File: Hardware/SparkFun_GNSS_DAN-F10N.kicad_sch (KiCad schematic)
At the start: 52 parts, among them J1 USB_C_Receptacle, J2 Conn_01x06, J4 U.FL, J5 Conn_01x08, U1 DT1042-04SO, U3 RT9080-3.3, U4 CH340C, U5 DAN-F10N

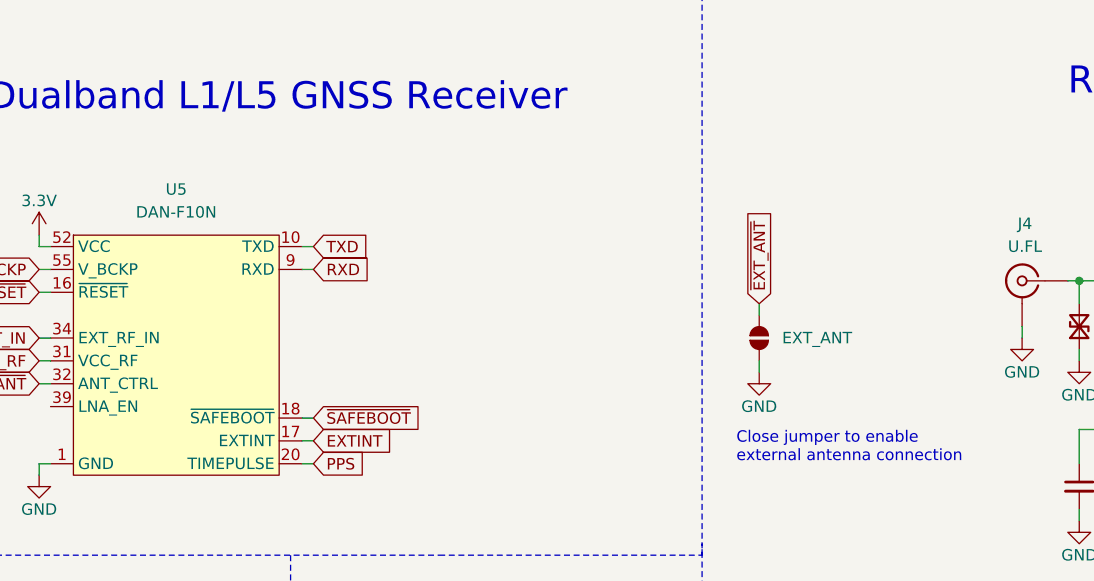
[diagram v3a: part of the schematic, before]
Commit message: Reduce paste on signal pads. Correct EXT_ANT activation level.
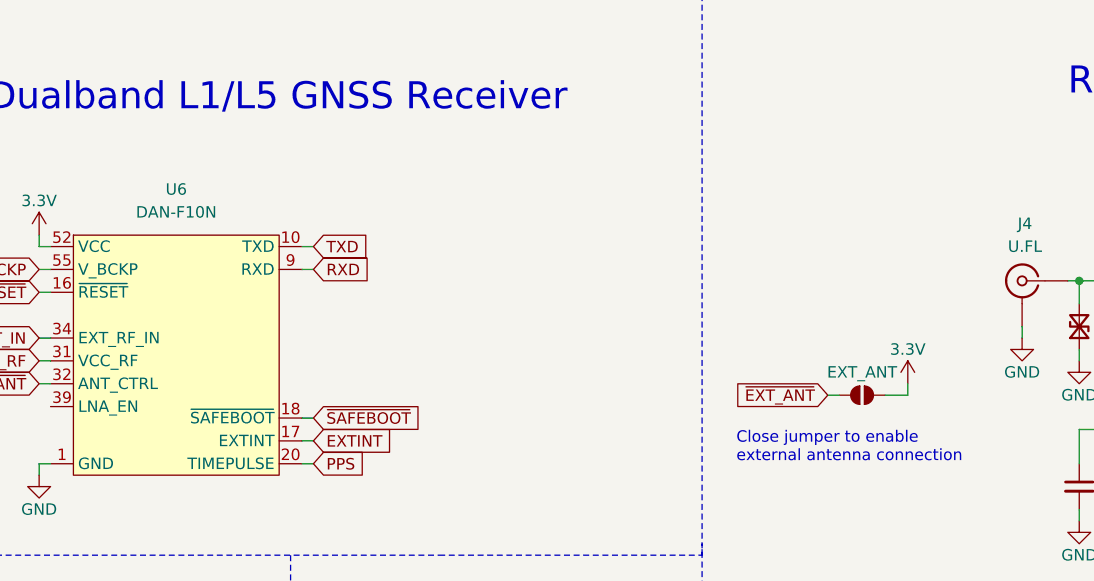
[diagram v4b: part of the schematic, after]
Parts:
- removed U5: DAN-F10N, SparkFun_GNSS_LG580P:DAN-F10N, symbol DAN-F10N:DAN-F10N
- added U6: DAN-F10N, DAN-F10N:DAN-F10N, symbol DAN-F10N:DAN-F10N
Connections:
- net 3.3V: now also JP1.1 (A), U6.52 (VCC), U6.53 (VCC)
- net ANT_IN: now also U6.34 (EXT_RF_IN)
- net EXTINT: now also U6.17 (EXTINT)
- net GND: now also U6.1 (GND), U6.13 (GND), U6.14 (GND), U6.15 (GND), U6.19 (GND), U6.2 (GND), U6.21 (GND), U6.22 (GND), U6.23 (GND), U6.26 (GND), U6.27 (GND), U6.28 (GND), U6.29 (GND), U6.3 (GND), U6.30 (GND), U6.33 (GND), U6.35 (GND), U6.37 (GND), U6.38 (GND), U6.4 (GND), U6.40 (GND), U6.41 (GND), U6.42 (GND), U6.43 (GND), U6.44 (GND), U6.47 (GND), U6.48 (GND), U6.49 (GND), U6.5 (GND), U6.50 (GND), U6.51 (GND), U6.54 (GND), U6.56 (GND), U6.57 (GND), U6.6 (GND), U6.7 (GND), U6.8 (GND); no longer JP1.1 (A)
- net PPS: now also U6.20 (TIMEPULSE)
- net RXD: now also U6.9 (RXD)
- net TXD: now also U6.10 (TXD)
- net VCC_RF: now also U6.31 (VCC_RF)
- net V_BCKP: now also U6.55 (V_BCKP)
- net ~{EXT_ANT}: now also U6.32 (ANT_CTRL)
- net ~{RESET}: now also U6.16 (~{RESET})
- net ~{SAFEBOOT}: now also U6.18 (~{SAFEBOOT})

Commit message: Add panel
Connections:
- net ~{EXT_ANT} renamed EXT_ANT
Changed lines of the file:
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@@
 		)
 	)
-	(global_label "~{EXT_ANT}"
+	(global_label "EXT_ANT"
 		(shape input)
 		(at 250.19 124.46 180)
@@
 		)
 	)
-	(global_label "~{EXT_ANT}"
+	(global_label "EXT_ANT"
 		(shape input)
 		(at 162.56 123.19 180)

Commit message: Remove local FP/SYM. Update to main kicad library.
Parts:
- U6: footprint DAN-F10N:DAN-F10N -> SparkFun-GNSS:u-blox_DAN-F10N; symbol DAN-F10N:DAN-F10N -> SparkFun-GNSS:DAN-F10N
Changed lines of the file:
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@@
 	)
 	(symbol
-		(lib_id "DAN-F10N:DAN-F10N")
+		(lib_id "SparkFun-GNSS:DAN-F10N")
 		(at 177.8 119.38 0)
 		(unit 1)
@@
 			)
 		)
-		(property "Footprint" "DAN-F10N:DAN-F10N"
+		(property "Footprint" "SparkFun-GNSS:u-blox_DAN-F10N"
 			(at 181.61 137.16 0)
 			(effects
